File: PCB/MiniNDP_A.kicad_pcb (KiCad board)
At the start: 2 copper layers, 60 x 34 mm, 25 parts, among them J1 Conn_02x20_Odd_Even, U1 HC161, U2 HC161, U3 HC161, U4 HC138, U5 HC374, U6 AS6C4008, U7 1G32, U8 1G79

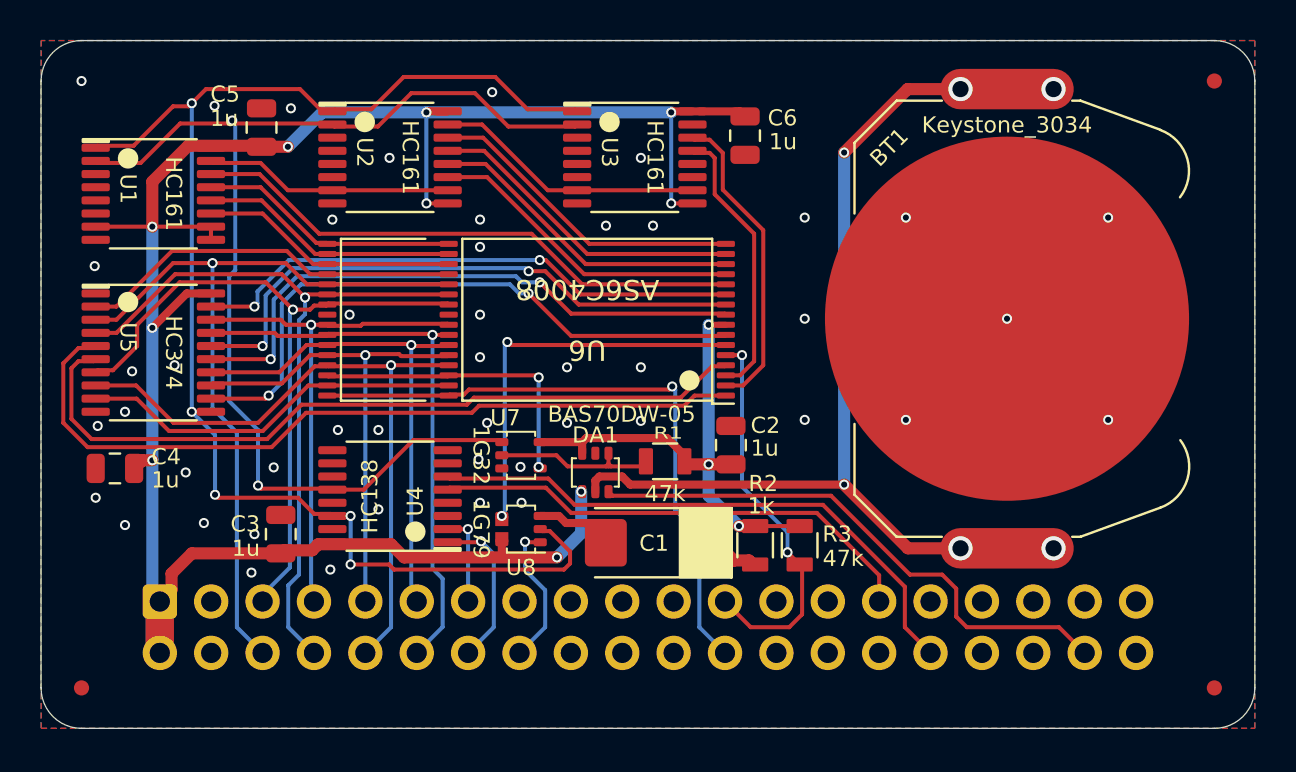
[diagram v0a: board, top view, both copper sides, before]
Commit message: make E version default, easier to solder
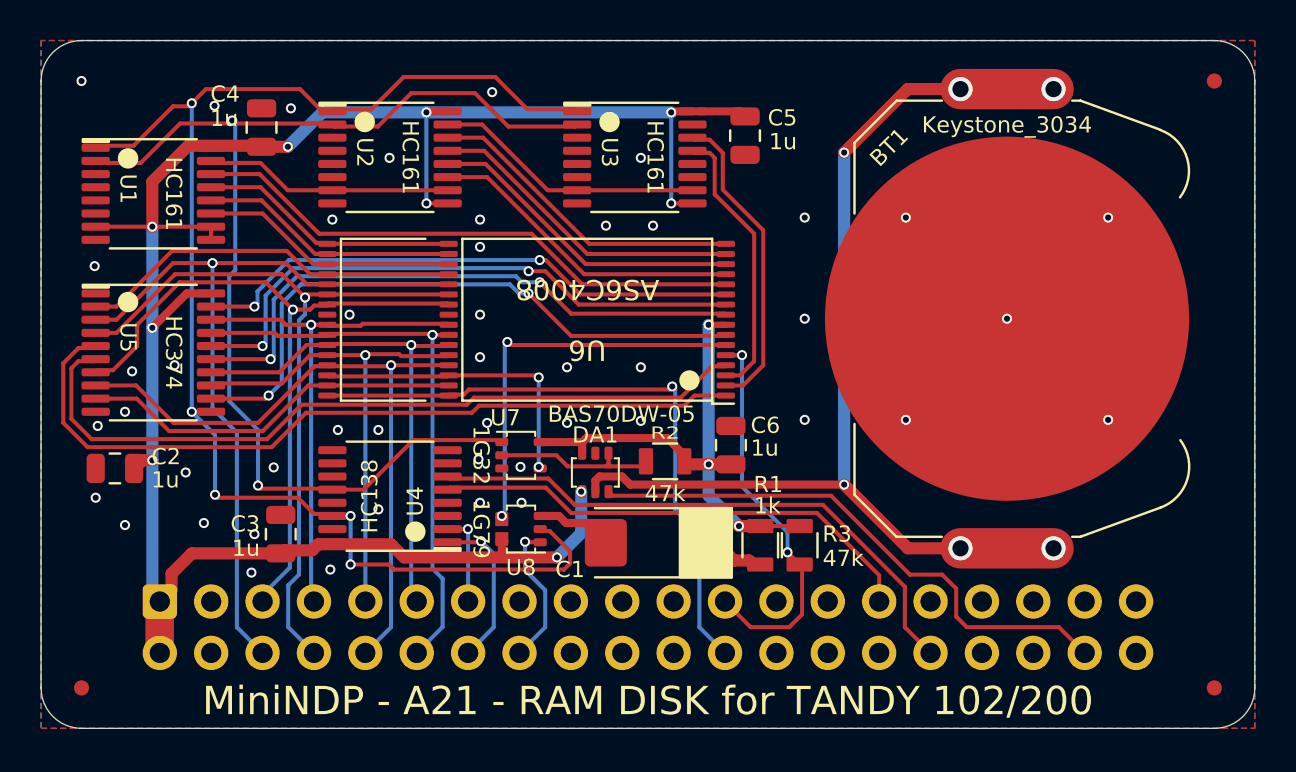
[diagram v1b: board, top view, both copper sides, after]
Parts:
- removed ENCLOSURE: MiniNDP_Cover, 000_LOCAL:MiniNDP_Cover
- added N1: MiniNDP_Cover, 000_LOCAL:MiniNDP_Cover, F.Cu at (151.9, 103.0)
- R1: value 47k -> 1k
- R2: value 1k -> 47k
- moved R1 6.27 mm to (157.5, 111.0), turned to -90 degrees
- moved R2 6.08 mm to (152.8, 106.8), turned to 180 degrees
- renumbered C4 to C2, C5 to C4, C6 to C5, C2 to C6
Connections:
- R1 pad 2: /SLEEP -> Net-(C1-Pad1)
- R2 pad 2: Net-(C1-Pad1) -> /SLEEP
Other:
- board text added: "${TITLE} - ${REVISION} - RAM DISK for TANDY 102/200"
- board text added: "100 1 CLEAR0,61558:T=61558:E=62957:OUT129,2 200 1 CLEAR0,59715:T=59715:E=61101:OUT129,2 2 FORA=0TO15:N=INP(131):NEXT:FORA=TTOE 3 POKEA,INP(131):IFA=T+1007THENOUT129,1 4 ?{dblquote}.{dblquote};:NEXT:SAVEM{dblquote}RAMDSK{dblquote},T,E,T"
- board text added: "Bootstrap RAMDSK from BANK 0. For BANK 1 change OUT129 to OUT133. RAM100.CO or RAM200.CO must be the first file in the bank."
- board text added: "RAM DISK for TANDY 102/200"
- board text removed: "cover"

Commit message: easy boards add 47u cap, remove ramrst diode
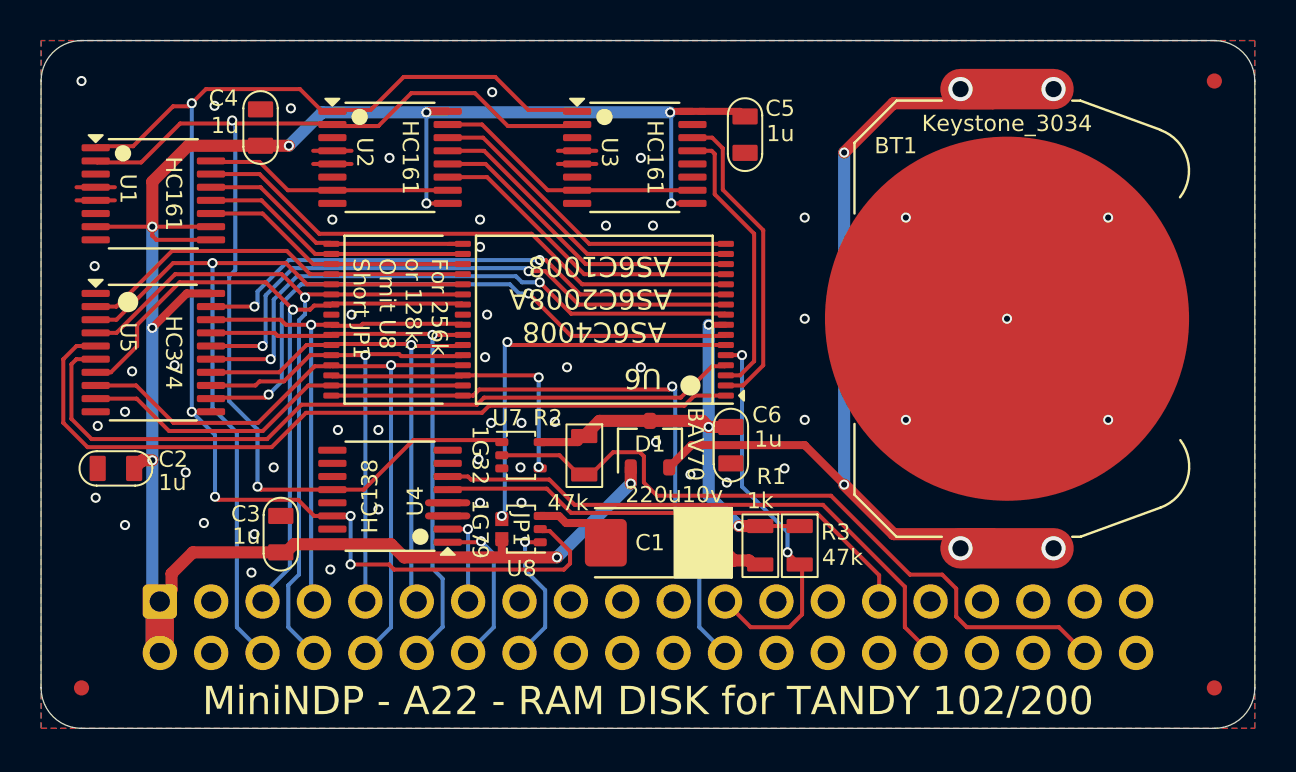
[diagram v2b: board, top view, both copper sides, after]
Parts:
- removed DA1: BAS70DW-05, 000_LOCAL:SOT-363_SC-70-6_symmetric
- added D1: BAV70, 000_LOCAL:SOT-23, F.Cu at (152.1, 106.0)
- moved R2 4.01 mm to (148.8, 106.5), turned to -90 degrees
- moved U6 3.35 mm to (149.3, 99.8)
- moved C2 0.05 mm to (125.7, 107.2)
- turned C6 to -90 degrees
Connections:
- R2 pad 2: /SLEEP -> /RAMRST
- U7 pad 2: /SLEEP -> /RAMRST
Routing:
- net GND: track 4.36 -> 19.6 mm, vias 47 -> 51
- net /SLEEP: track 8.46 -> 0.00 mm
- net /RAMRST: track 27.7 -> 35.3 mm
- net VBUS: track 105.8 -> 110.7 mm
- net +BATT: track 48.3 -> 45.0 mm
- net /A1: track 12.9 -> 14.5 mm
- net VMEM: track 25.2 -> 24.4 mm
- net /AD7: track 25.2 -> 25.9 mm
- net /AD6: track 28.3 -> 29.0 mm
- net /AD0: track 39.3 -> 40.0 mm
- net /A3: track 12.8 -> 13.5 mm
- net /A2: track 12.8 -> 13.5 mm
- net /A14: track 19.0 -> 19.7 mm
- net /A10: track 19.1 -> 19.8 mm
- net /AD5: track 24.6 -> 25.3 mm
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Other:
- board text added: "AS6C2008A AS6C1008"
- board text added: "For 256k or 128k: Omit U8 Short JP1"
